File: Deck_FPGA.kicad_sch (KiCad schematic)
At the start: 72 parts, among them J1 Left side, J2 Right Side, J3 Conn_01x06, U1 XC7A100T-CSG324, U2 TPS65023BRSBT, U3 S25FL128SAGNFI000, U4 LM3880, X1 ASE-100MHz

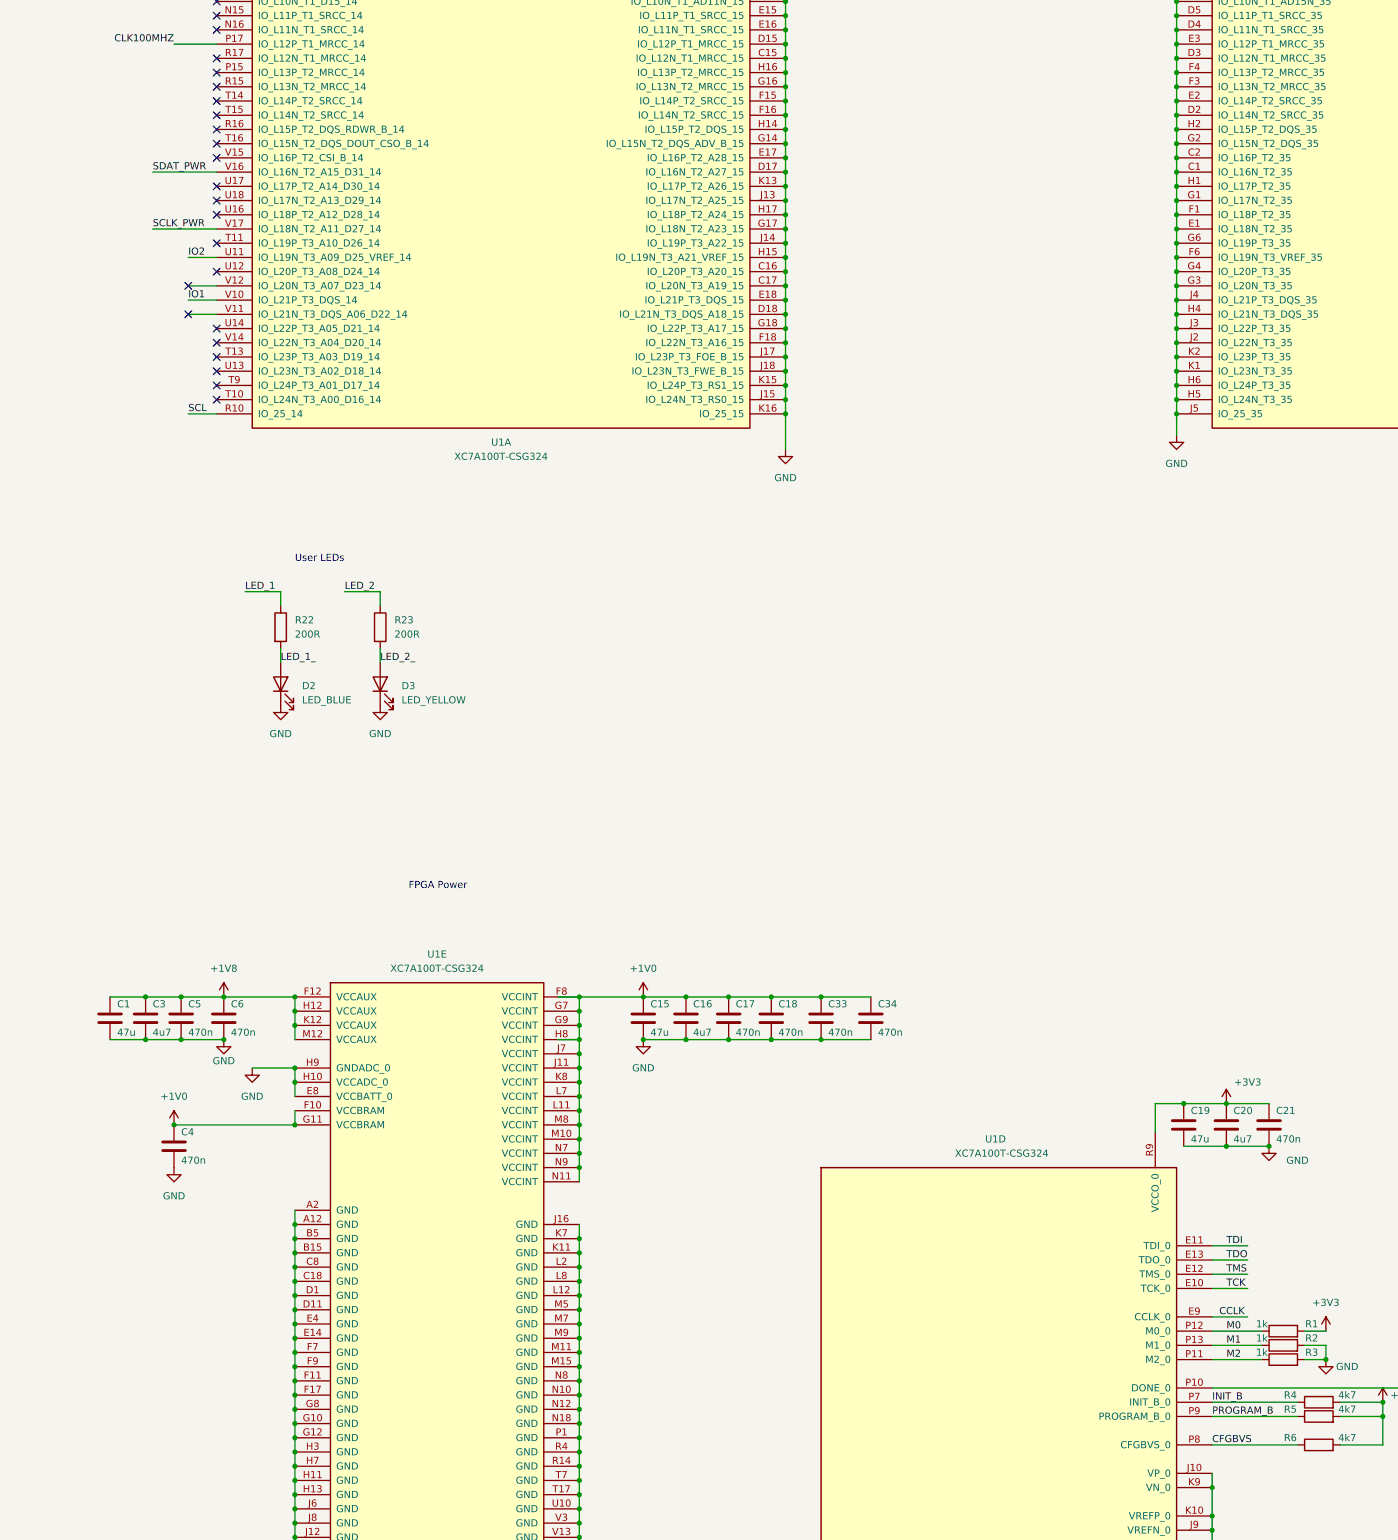
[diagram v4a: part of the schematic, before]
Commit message: added testpad for program_b and user switch
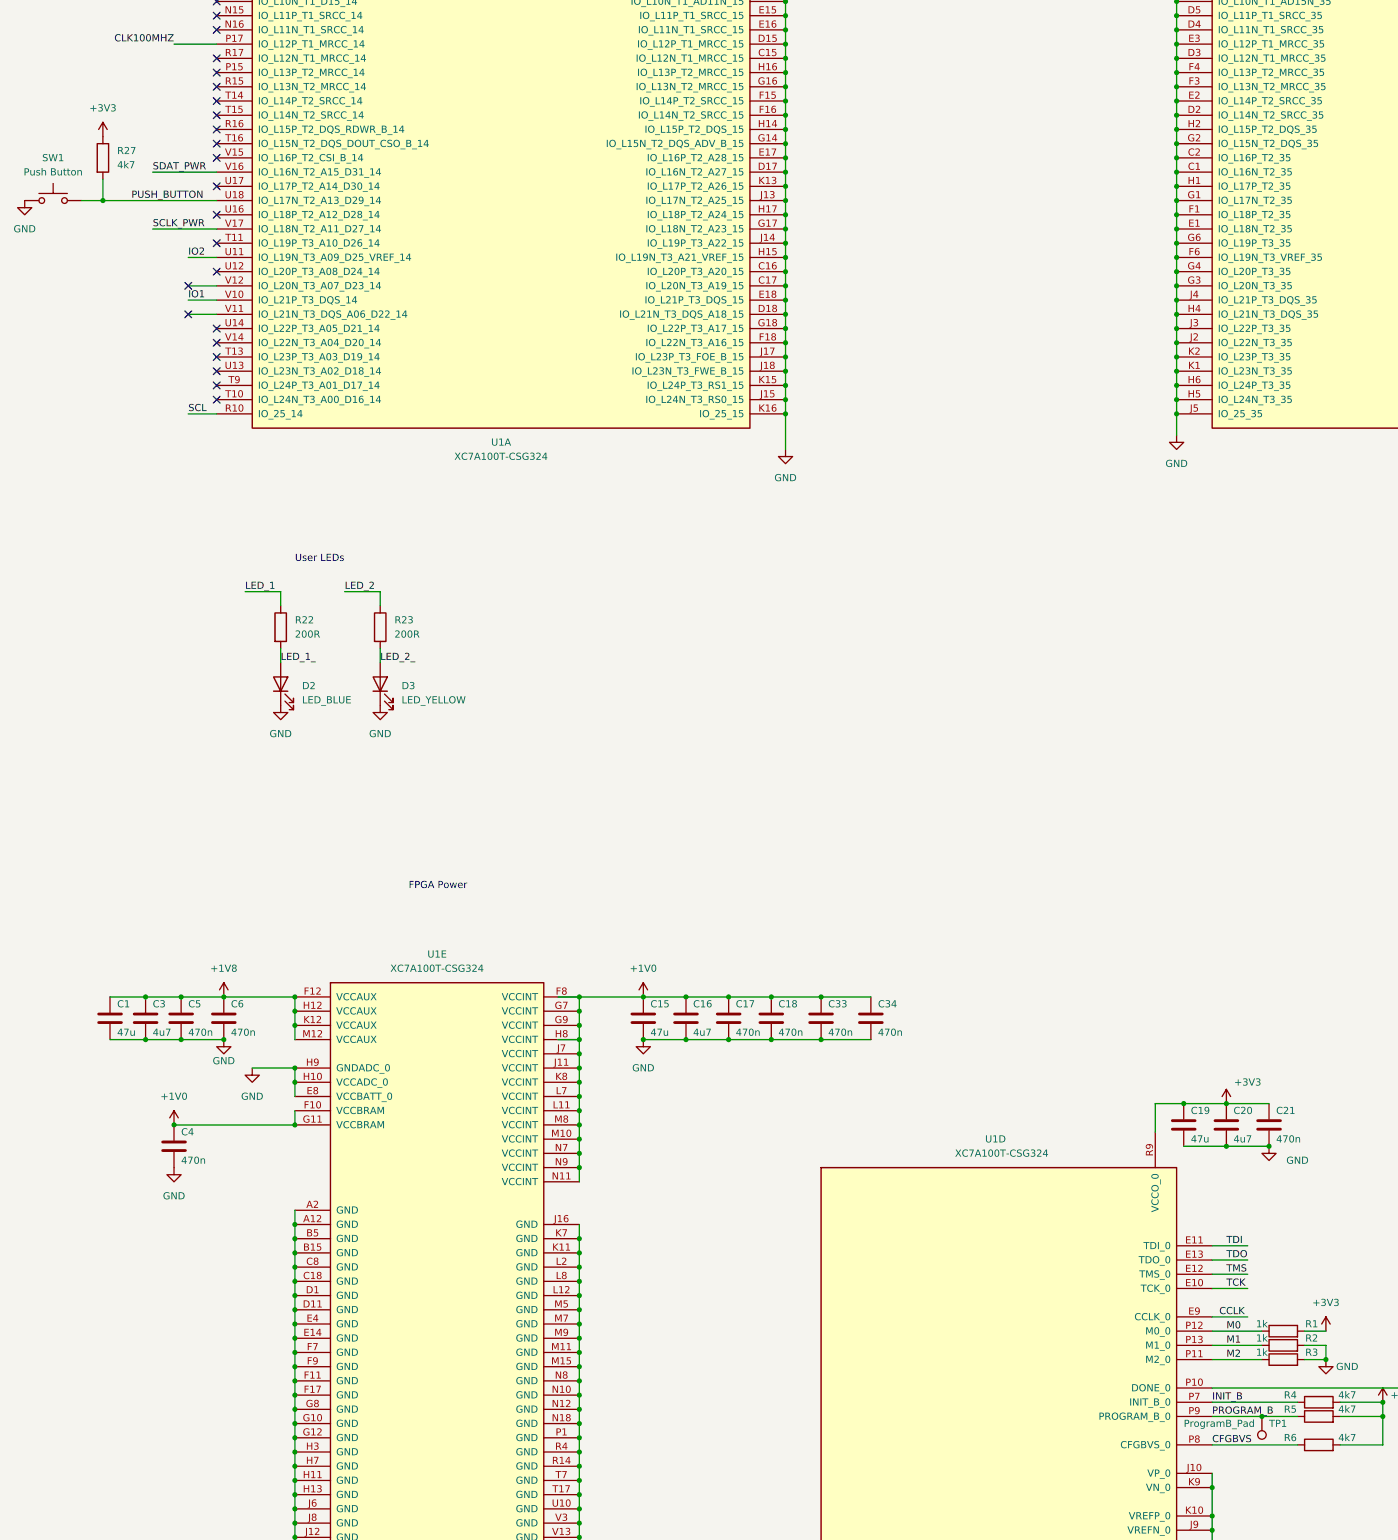
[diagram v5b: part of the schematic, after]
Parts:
- added R27: 4k7, Resistor_SMD:R_0402_1005Metric, symbol Device:R
- added SW1: Push Button, power_ic:SW_EVQ-P3401P, symbol Switch:SW_Push
- added TP1: ProgramB_Pad, TestPoint:TestPoint_Pad_D1.0mm, symbol Connector:TestPoint
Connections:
- net +3V3: now also R27.1
- net GND: now also SW1.1
- net PROGRAM_B: now also TP1.1
- net PUSH_BUTTON: now reaches U1.U18 (IO_L17N_T2_A13_D29_14)
- net PUSH_BUTTON: now also R27.2, SW1.2
- no-connect marks 39 -> 38
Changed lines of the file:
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@@
   (junction (at 114.3 356.87) (diameter 0) (color 0 0 0 0)
   )
+  (junction (at 236.22 353.06) (diameter 0) (color 0 0 0 0)
+  )
   (junction (at 151.13 148.59) (diameter 0) (color 0 0 0 0)
   )
@@
   (junction (at 233.68 29.21) (diameter 0) (color 0 0 0 0)
   )
+  (junction (at 29.21 135.89) (diameter 0) (color 0 0 0 0)
+  )
   (junction (at 410.21 364.49) (diameter 0) (color 0 0 0 0)
   )
@@
   (no_connect (at 49.53 74.93))
   (no_connect (at 49.53 158.75))
-  (no_connect (at 49.53 135.89))
   (no_connect (at 339.09 242.57))
   (no_connect (at 49.53 113.03))
@@
     (stroke (width 0) (type default) (color 0 0 0 0))
   )
+  (wire (pts (xy 236.22 353.06) (xy 242.57 353.06))
+    (stroke (width 0) (type default) (color 0 0 0 0))
+  )
   (wire (pts (xy 217.17 302.26) (xy 217.17 297.18))
     (stroke (width 0) (type default) (color 0 0 0 0))
@@
     (stroke (width 0) (type default) (color 0 0 0 0))
   )
-  (wire (pts (xy 227.33 353.06) (xy 242.57 353.06))
-    (stroke (width 0) (type default) (color 0 0 0 0))
-  )
   (wire (pts (xy 49.53 62.23) (xy 24.13 62.23))
     (stroke (width 0) (type default) (color 0 0 0 0))
@@
     (stroke (width 0) (type default) (color 0 0 0 0))
   )
+  (wire (pts (xy 227.33 353.06) (xy 236.22 353.06))
+    (stroke (width 0) (type default) (color 0 0 0 0))
+  )
   (wire (pts (xy 151.13 54.61) (xy 151.13 57.15))
     (stroke (width 0) (type default) (color 0 0 0 0))
@@
     (stroke (width 0) (type default) (color 0 0 0 0))
   )
+  (wire (pts (xy 29.21 135.89) (xy 49.53 135.89))
+    (stroke (width 0) (type default) (color 0 0 0 0))
+  )
   (wire (pts (xy 548.64 356.87) (xy 557.53 356.87))
     (stroke (width 0) (type default) (color 0 0 0 0))
   )
+  (wire (pts (xy 25.4 135.89) (xy 29.21 135.89))
+    (stroke (width 0) (type default) (color 0 0 0 0))
+  )
   (wire (pts (xy 71.12 17.78) (xy 86.36 17.78))
     (stroke (width 0) (type default) (color 0 0 0 0))
@@
     (stroke (width 0) (type default) (color 0 0 0 0))
   )
+  (wire (pts (xy 29.21 132.08) (xy 29.21 135.89))
+    (stroke (width 0) (type default) (color 0 0 0 0))
+  )
   (wire (pts (xy 220.98 72.39) (xy 220.98 74.93))
     (stroke (width 0) (type default) (color 0 0 0 0))
@@
     (effects (font (size 1.27 1.27)) (justify left bottom))
   )
+  (label "PUSH_BUTTON" (at 34.29 135.89 0)
+    (effects (font (size 1.27 1.27)) (justify left bottom))
+  )
   (label "SCL" (at 44.45 173.99 0)
     (effects (font (size 1.27 1.27)) (justify left bottom))
@@
     (pin "2")
   )
+  (symbol (lib_id "power:GND") (at 15.24 135.89 0) (unit 1)
+    (in_bom yes) (on_board yes) (fields_autoplaced)
+    (property "Reference" "#PWR059" (id 0) (at 15.24 142.24 0)
+      (effects (font (size 1.27 1.27)) hide)
+    )
+    (property "Value" "GND" (id 1) (at 15.24 140.97 0))
+    (property "Footprint" "" (id 2) (at 15.24 135.89 0)
+      (effects (font (size 1.27 1.27)) hide)
+    )
+    (property "Datasheet" "" (id 3) (at 15.24 135.89 0)
+      (effects (font (size 1.27 1.27)) hide)
+    )
+    (pin "1")
+  )
   (symbol (lib_id "Connector_Generic:Conn_01x10") (at 350.52 232.41 0) (unit 1)
     (in_bom yes) (on_board yes)
@@
     (pin "1")
   )
+  (symbol (lib_id "Connector:TestPoint") (at 236.22 353.06 180) (unit 1)
+    (in_bom yes) (on_board yes)
+    (property "Reference" "TP1" (id 0) (at 237.49 354.33 0)
+      (effects (font (size 1.27 1.27)) (justify right))
+    )
+    (property "Value" "ProgramB_Pad" (id 1) (at 222.25 354.33 0)
+      (effects (font (size 1.27 1.27)) (justify right))
+    )
+    (property "Footprint" "TestPoint:TestPoint_Pad_D1.0mm" (id 2) (at 231.14 353.06 0)
+      (effects (font (size 1.27 1.27)) hide)
+    )
+    (property "Datasheet" "~" (id 3) (at 231.14 353.06 0)
+      (effects (font (size 1.27 1.27)) hide)
+    )
+    (pin "1")
+  )
   (symbol (lib_id "Device:R") (at 278.13 344.17 0) (unit 1)
     (in_bom yes) (on_board yes) (fields_autoplaced)
@@
     (pin "2")
   )
+  (symbol (lib_id "power:+3V3") (at 29.21 124.46 0) (unit 1)
+    (in_bom yes) (on_board yes) (fields_autoplaced)
+    (property "Reference" "#PWR060" (id 0) (at 29.21 128.27 0)
+      (effects (font (size 1.27 1.27)) hide)
+    )
+    (property "Value" "+3V3" (id 1) (at 29.21 119.38 0))
+    (property "Footprint" "" (id 2) (at 29.21 124.46 0)
+      (effects (font (size 1.27 1.27)) hide)
+    )
+    (property "Datasheet" "" (id 3) (at 29.21 124.46 0)
+      (effects (font (size 1.27 1.27)) hide)
+    )
+    (pin "1")
+  )
   (symbol (lib_id "Device:C") (at 486.41 309.88 0) (unit 1)
     (in_bom yes) (on_board yes)
@@
     (pin "2")
   )
+  (symbol (lib_id "Switch:SW_Push") (at 20.32 135.89 0) (unit 1)
+    (in_bom yes) (on_board yes) (fields_autoplaced)
+    (property "Reference" "SW1" (id 0) (at 20.32 128.27 0))
+    (property "Value" "Push Button" (id 1) (at 20.32 130.81 0))
+    (property "Footprint" "power_ic:SW_EVQ-P3401P" (id 2) (at 20.32 130.81 0)
+      (effects (font (size 1.27 1.27)) hide)
+    )
+    (property "Datasheet" "~" (id 3) (at 20.32 130.81 0)
+      (effects (font (size 1.27 1.27)) hide)
+    )
+    (property "LCSC" "C79163" (id 4) (at 20.32 135.89 0)
+      (effects (font (size 1.27 1.27)) hide)
+    )
+    (pin "1")
+    (pin "2")
+  )
   (symbol (lib_id "power:GND") (at 322.58 355.6 0) (unit 1)
     (in_bom yes) (on_board yes) (fields_autoplaced)
@@
     (pin "1")
   )
+  (symbol (lib_id "Device:R") (at 29.21 128.27 0) (unit 1)
+    (in_bom yes) (on_board yes) (fields_autoplaced)
+    (property "Reference" "R27" (id 0) (at 31.75 126.9999 0)
+      (effects (font (size 1.27 1.27)) (justify left))
+    )
+    (property "Value" "4k7" (id 1) (at 31.75 129.5399 0)
+      (effects (font (size 1.27 1.27)) (justify left))
+    )
+    (property "Footprint" "Resistor_SMD:R_0402_1005Metric" (id 2) (at 27.432 128.27 90)
+      (effects (font (size 1.27 1.27)) hide)
+    )
+    (property "Datasheet" "~" (id 3) (at 29.21 128.27 0)
+      (effects (font (size 1.27 1.27)) hide)
+    )
+    (pin "1")
+    (pin "2")
+  )
   (symbol (lib_id "Device:C") (at 71.12 21.59 0) (unit 1)
     (in_bom yes) (on_board yes)
@@
       (reference "#PWR058") (unit 1) (value "+3V3") (footprint "")
     )
+    (path "/13ac9377-dc55-4e6b-b25e-08abd131539c"
+      (reference "#PWR059") (unit 1) (value "GND") (footprint "")
+    )
+    (path "/850ce185-27d6-4969-a1c8-006f3457171e"
+      (reference "#PWR060") (unit 1) (value "+3V3") (footprint "")
+    )
     (path "/22a99473-3e55-4b82-8223-740f01d7295e"
       (reference "C1") (unit 1) (value "47u") (footprint "Capacitor_SMD:C_0603_1608Metric")
@@
       (reference "R26") (unit 1) (value "10R") (footprint "Resistor_SMD:R_0402_1005Metric")
     )
+    (path "/bc8f3fa9-b144-4b23-8a77-93b56b19e105"
+      (reference "R27") (unit 1) (value "4k7") (footprint "Resistor_SMD:R_0402_1005Metric")
+    )
+    (path "/ba62a20f-b5d3-4611-80cc-f6c551c956b4"
+      (reference "SW1") (unit 1) (value "Push Button") (footprint "power_ic:SW_EVQ-P3401P")
+    )
+    (path "/3d2b829c-dd56-4e6a-aa8f-d7d27ae72489"
+      (reference "TP1") (unit 1) (value "ProgramB_Pad") (footprint "TestPoint:TestPoint_Pad_D1.0mm")
+    )
     (path "/ecc74e25-e331-48ee-bb2b-1cee9992f2cd"
